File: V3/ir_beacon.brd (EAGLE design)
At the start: 50.8 x 38.1 mm, 35 parts, among them J2 B-, J3 B+, SW1 CNK-L202_MS02, U1 555_TIMER_DIP8

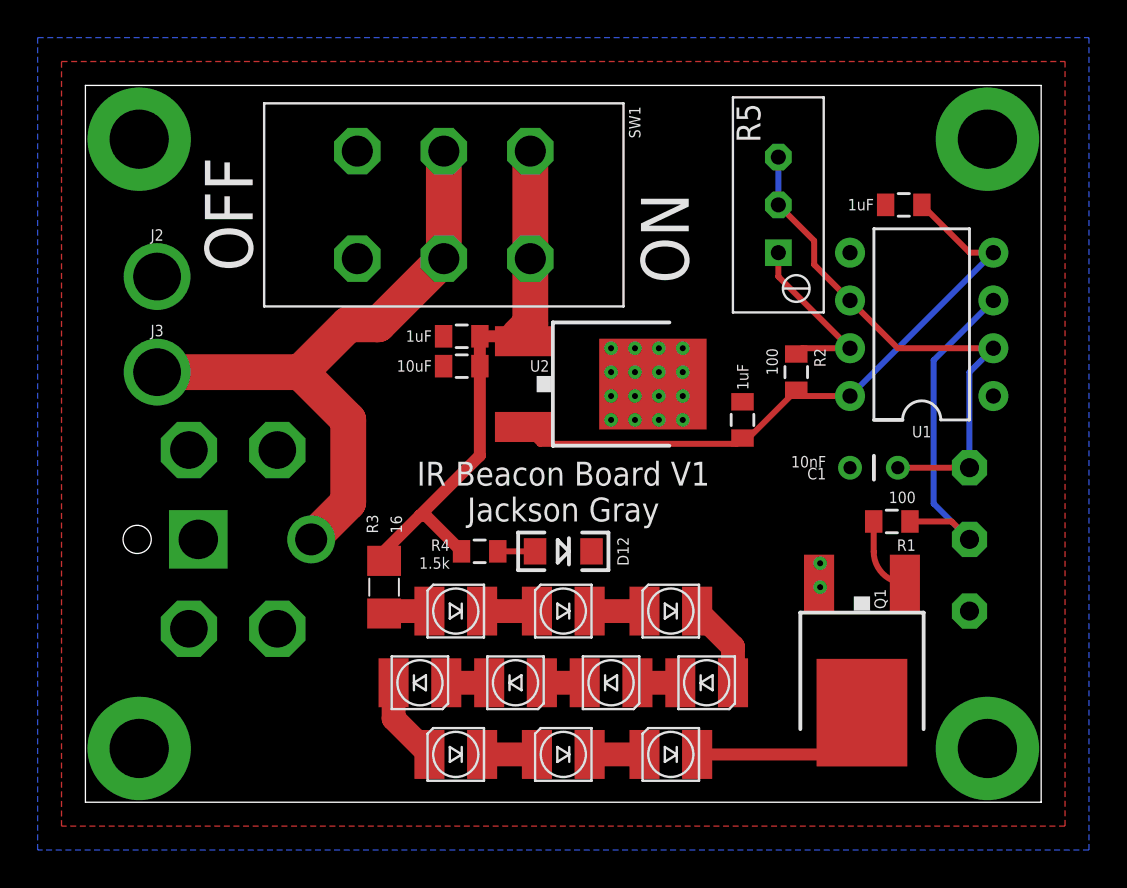
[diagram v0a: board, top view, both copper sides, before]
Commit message: Changed the testpoint type slightly, added a few more to the board. Moved around some traces and added many more vias for thermal conductivity. Generated new gerbers for the beacon board.
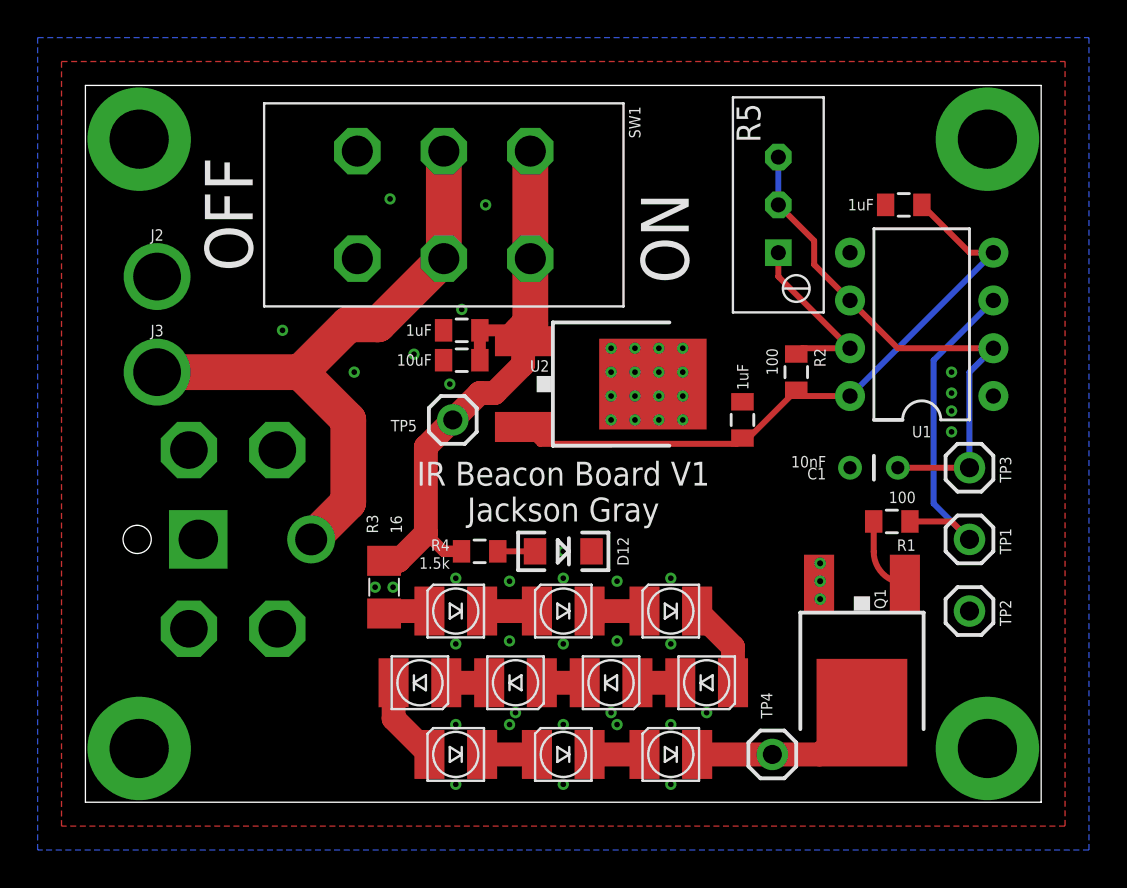
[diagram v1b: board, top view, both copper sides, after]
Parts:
- added TP4: LED-, meltylib:1X01
- added TP5: LED+, meltylib:1X01
- TP1, TP2, TP3: device jack_electromechanical:TEST_POINT -> meltylib:1X01
- moved C5 0.32 mm to (20.0, 23.5)
- moved C4 0.32 mm to (20.0, 25.1)
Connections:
- net 555CAP: now also TP3.1; no longer TP3.P
- net GND: now also TP2.1; no longer TP2.P
- net N$11: now also TP4.1
- net N$16: now also TP1.1; no longer TP1.P
- net V_BATT: now also TP5.1
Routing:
- net V_BATT: track 29.6 -> 32.4 mm
